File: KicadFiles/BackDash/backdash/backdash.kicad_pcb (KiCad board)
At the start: 2 copper layers, 92.7 x 67.3 mm, 11 parts

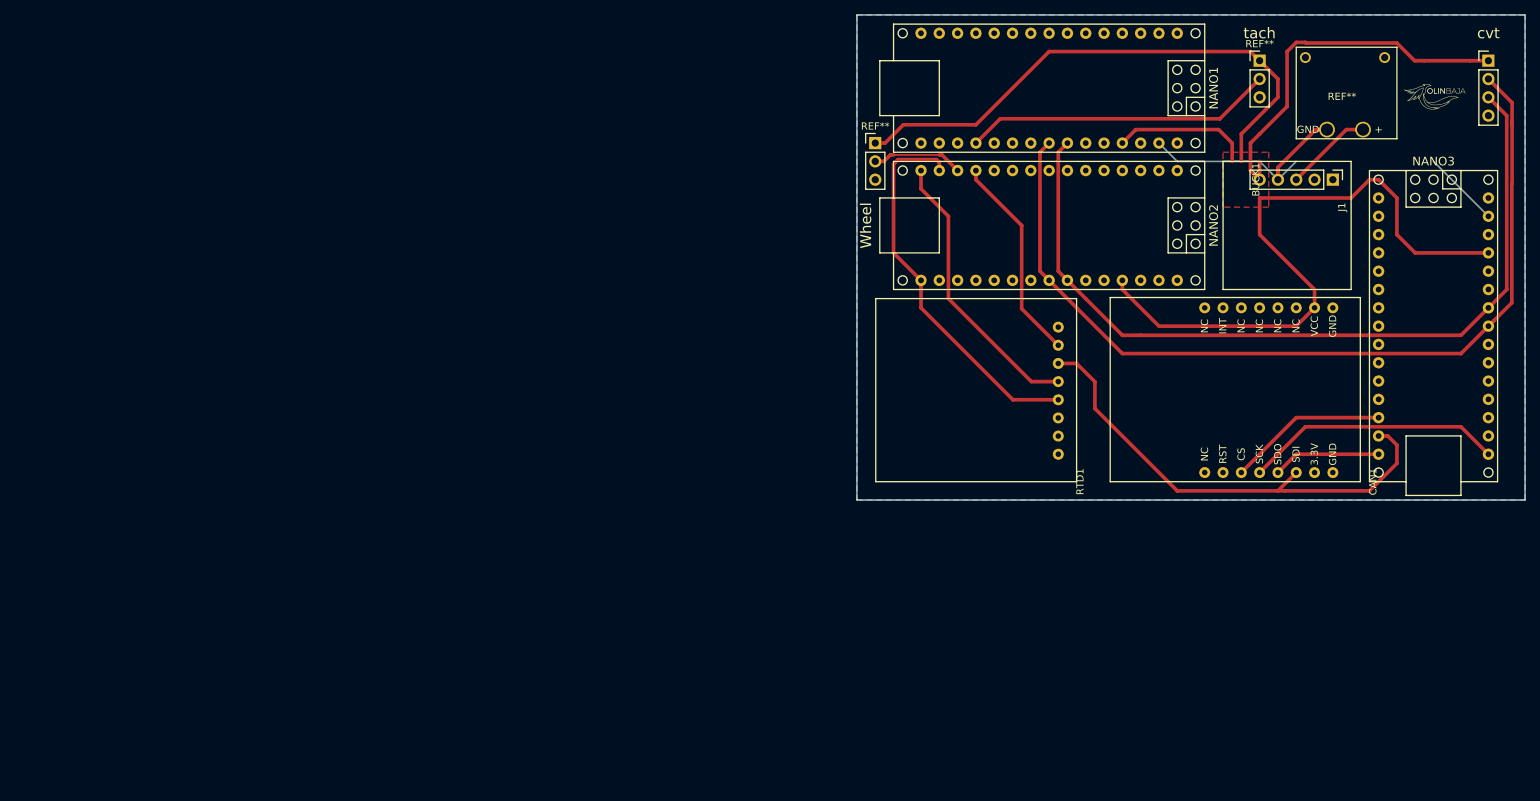
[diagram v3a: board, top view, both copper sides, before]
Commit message: added tach sechematic, needs buck footprint
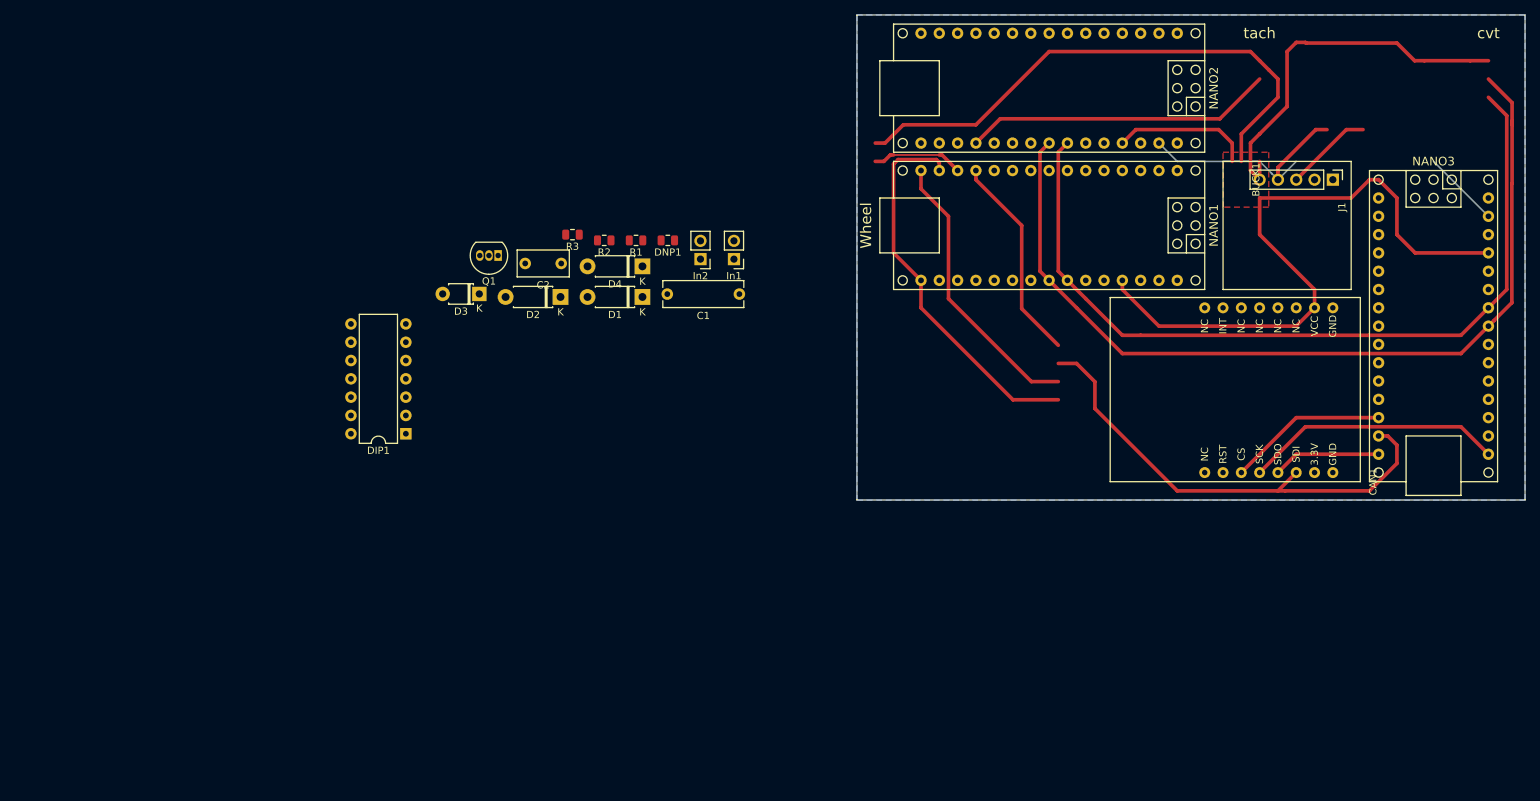
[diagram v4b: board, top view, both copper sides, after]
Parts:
- removed G***: LOGO, TestBaja:Baja_Logo_Tach
- removed REF** (x2): Pin_Header_Straight_1x03_Pitch2.54mm, Pin_Headers:Pin_Header_Straight_1x03_Pitch2.54mm
- removed REF**: Pin_Header_Straight_1x04_Pitch2.54mm, Pin_Headers:Pin_Header_Straight_1x04_Pitch2.54mm
- removed REF**: DC_Connector, TestBaja:DC_Connector
- removed RTD1: Conn_01x08_Female, TestBaja:RTD
- added C1: 2200pF, Capacitor_THT:C_Rect_L11.0mm_W3.5mm_P10.00mm_MKT, F.Cu at (146.2, 60.3)
- added C2: 39nF, Capacitor_THT:C_Rect_L7.0mm_W3.5mm_P5.00mm, F.Cu at (121.5, 56.1)
- added D1: 1N4007, Diode_THT:D_DO-41_SOD81_P7.62mm_Horizontal, F.Cu at (132.8, 60.7)
- added D2: 1N4007, Diode_THT:D_DO-41_SOD81_P7.62mm_Horizontal, F.Cu at (121.4, 60.7)
- added D3: 1N4148, Diode_THT:D_T-1_P5.08mm_Horizontal, F.Cu at (110.2, 60.3)
- added D4: 1N4738, Diode_THT:D_DO-41_SOD81_P7.62mm_Horizontal, F.Cu at (132.8, 56.5)
- added DIP1: SN74HC14N, Package_DIP:DIP-14_W7.62mm, F.Cu at (100.0, 79.7)
- added DNP1: DNP, Resistor_SMD:R_0805_2012Metric, F.Cu at (136.3, 52.9)
- added In1: Vin +, Connector_PinHeader_2.54mm:PinHeader_1x02_P2.54mm_Vertical, F.Cu at (145.5, 55.5)
- added In2: Vin-, Connector_PinHeader_2.54mm:PinHeader_1x02_P2.54mm_Vertical, F.Cu at (140.8, 55.5)
- added Q1: 2N3904, Package_TO_SOT_THT:TO-92_Inline, F.Cu at (112.8, 55.0)
- added R1: 10k, Resistor_SMD:R_0805_2012Metric, F.Cu at (131.9, 52.9)
- added R2: 10k, Resistor_SMD:R_0805_2012Metric, F.Cu at (127.5, 52.9)
- added R3: 4.7k, Resistor_SMD:R_0805_2012Metric, F.Cu at (123.1, 52.1)
- renumbered NANO2 to NANO1, NANO1 to NANO2
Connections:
- net Net-(CAN1-Pad10) renamed /INT
- BUCK1 pad 3: /IN -> Net-(BUCK1-Pad3)
- BUCK1 pad 4: /GND -> Net-(BUCK1-Pad4)
- BUCK1 pad 5: /VCC -> Net-(BUCK1-Pad5)
- CAN1 pad 1: Net-(CAN1-Pad1) -> /GND
- CAN1 pad 11: Net-(CAN1-Pad11) -> /NC
- CAN1 pad 12: Net-(CAN1-Pad12) -> /NC
- CAN1 pad 13: Net-(CAN1-Pad13) -> /NC
- CAN1 pad 14: Net-(CAN1-Pad14) -> /NC
- CAN1 pad 2: /3V3 -> /3.3V
- CAN1 pad 4: /SDOcan -> /SDO
- CAN1 pad 6: /CScan -> /CS
- CAN1 pad 7: Net-(CAN1-Pad7) -> /RST
- CAN1 pad 8: Net-(CAN1-Pad8) -> /NC
- CAN1 pad 9: Net-(CAN1-Pad9) -> /NC
- NANO1 pad 1: Net-(NANO2-Pad1) -> /TX1
- NANO1 pad 10: Net-(NANO2-Pad10) -> /D7
- NANO1 pad 11: Net-(NANO2-Pad11) -> /D8
- NANO1 pad 12: /CSrtd -> /D9
- NANO1 pad 14: /CLK -> /D11
- NANO1 pad 15: /SDOrtd -> /D12
- NANO1 pad 16: /CLK -> /D13
- NANO1 pad 17: Net-(NANO2-Pad17) -> /3.3V
- NANO1 pad 18: Net-(NANO2-Pad18) -> /REF
- NANO1 pad 19: Net-(NANO2-Pad19) -> /A0
- NANO1 pad 2: Net-(NANO2-Pad2) -> /RX0
- NANO1 pad 20: Net-(NANO2-Pad20) -> /A1
- NANO1 pad 21: Net-(NANO2-Pad21) -> /A2
- NANO1 pad 22: Net-(NANO2-Pad22) -> /A3
- NANO1 pad 25: Net-(NANO2-Pad25) -> /A6
- NANO1 pad 26: Net-(NANO2-Pad26) -> /A7
- NANO1 pad 28: Net-(NANO2-Pad28) -> /RST
- NANO1 pad 3: Net-(NANO2-Pad3) -> /RST
- NANO1 pad 30: Net-(NANO2-Pad30) -> /VIN
- NANO1 pad 4: Net-(NANO2-Pad4) -> /GND
- NANO1 pad 5: Net-(NANO2-Pad5) -> /D2
- NANO1 pad 6: Net-(NANO2-Pad6) -> /D3
- NANO1 pad 7: Net-(NANO2-Pad7) -> /D4
- NANO1 pad 8: Net-(NANO2-Pad8) -> /D5
- NANO1 pad 9: Net-(NANO2-Pad9) -> /D6
- NANO2 pad 1: Net-(NANO1-Pad1) -> /TX1
- NANO2 pad 10: Net-(NANO1-Pad10) -> /D7
- NANO2 pad 11: Net-(NANO1-Pad11) -> /D8
- NANO2 pad 12: Net-(NANO1-Pad12) -> /D9
- NANO2 pad 13: Net-(NANO1-Pad13) -> /D10
- NANO2 pad 14: Net-(NANO1-Pad14) -> /D11
- NANO2 pad 15: Net-(NANO1-Pad15) -> /D12
- NANO2 pad 16: Net-(NANO1-Pad16) -> /D13
- NANO2 pad 17: Net-(NANO1-Pad17) -> /3.3V
- NANO2 pad 18: Net-(NANO1-Pad18) -> /REF
- NANO2 pad 2: Net-(NANO1-Pad2) -> /RX0
- NANO2 pad 20: Net-(NANO1-Pad20) -> /A1
- NANO2 pad 21: Net-(NANO1-Pad21) -> /A2
- NANO2 pad 22: Net-(NANO1-Pad22) -> /A3
- NANO2 pad 25: Net-(NANO1-Pad25) -> /A6
- NANO2 pad 26: Net-(NANO1-Pad26) -> /A7
- NANO2 pad 28: Net-(NANO1-Pad28) -> /RST
- NANO2 pad 3: Net-(NANO1-Pad3) -> /RST
- NANO2 pad 30: Net-(NANO1-Pad30) -> /VIN
- NANO2 pad 4: Net-(NANO1-Pad4) -> /GND
- NANO2 pad 5: Net-(NANO1-Pad5) -> /D2
- NANO2 pad 6: Net-(NANO1-Pad6) -> /D3
- NANO2 pad 7: Net-(NANO1-Pad7) -> /D4
- NANO2 pad 8: Net-(NANO1-Pad8) -> /D5
- NANO2 pad 9: Net-(NANO1-Pad9) -> /D6
- NANO3 pad 1: Net-(NANO3-Pad1) -> /TX1
- NANO3 pad 10: Net-(NANO3-Pad10) -> /D7
- NANO3 pad 11: Net-(NANO3-Pad11) -> /D8
- NANO3 pad 12: Net-(NANO3-Pad12) -> /D9
- NANO3 pad 13: /CScan -> /D10
- NANO3 pad 14: /SDI -> /D11
- NANO3 pad 15: /SDOcan -> /D12
- NANO3 pad 16: /SCK -> /D13
- NANO3 pad 17: Net-(NANO3-Pad17) -> /3.3V
- NANO3 pad 18: Net-(NANO3-Pad18) -> /REF
- NANO3 pad 19: Net-(NANO3-Pad19) -> /A0
- NANO3 pad 2: Net-(NANO3-Pad2) -> /RX0
- NANO3 pad 20: Net-(NANO3-Pad20) -> /A1
- NANO3 pad 21: Net-(NANO3-Pad21) -> /A2
- NANO3 pad 22: Net-(NANO3-Pad22) -> /A3
- NANO3 pad 25: Net-(NANO3-Pad25) -> /A6
- NANO3 pad 26: Net-(NANO3-Pad26) -> /A7
- NANO3 pad 28: Net-(NANO3-Pad28) -> /RST
- NANO3 pad 3: Net-(NANO3-Pad3) -> /RST
- NANO3 pad 30: Net-(NANO3-Pad30) -> /VIN
- NANO3 pad 4: Net-(NANO3-Pad4) -> /GND
- NANO3 pad 5: Net-(NANO3-Pad5) -> /D2
- NANO3 pad 6: Net-(NANO3-Pad6) -> /D3
- NANO3 pad 7: Net-(NANO3-Pad7) -> /D4
- NANO3 pad 8: Net-(NANO3-Pad8) -> /D5
- NANO3 pad 9: Net-(NANO3-Pad9) -> /D6
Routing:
- net Net-(BUCK1-Pad5): track 0.00 -> 52.5 mm
- net /VCC: track 237.5 -> 185.1 mm
- net /SDOrtd: track 39.4 -> 0.00 mm
- net /D12: track 0.00 -> 39.4 mm
- net /D9: track 0.00 -> 29.0 mm
- net /CSrtd: track 29.0 -> 0.00 mm
- net /D11: track 0.00 -> 23.7 mm
- net /SDI: track 67.3 -> 43.6 mm
- net Net-(BUCK1-Pad3): track 0.00 -> 12.1 mm
- net /IN: track 12.1 -> 0.00 mm

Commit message: updating backdash
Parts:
- added REF**: DC_Connector, TestBaja:DC_Connector, F.Cu at (215.9, 38.1)
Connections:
- BUCK1 pad 4: Net-(BUCK1-Pad4) -> /GND
- BUCK1 pad 5: Net-(BUCK1-Pad5) -> /VCC
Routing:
- net /VCC: track 185.1 -> 111.9 mm
- net Net-(BUCK1-Pad5): track 52.5 -> 0.00 mm
- net /GND: track 43.7 -> 33.0 mm
- net /A0: track 43.1 -> 35.2 mm
- net Net-(BUCK1-Pad3): track 12.1 -> 6.51 mm
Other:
- board text removed: "cvt"
- board text removed: "tach"
